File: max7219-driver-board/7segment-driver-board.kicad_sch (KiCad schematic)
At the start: 10 parts, among them IC1 MAX7219CWG, P1 Ext PWR, P2 DataIn, P3 DataOut, P4 Display

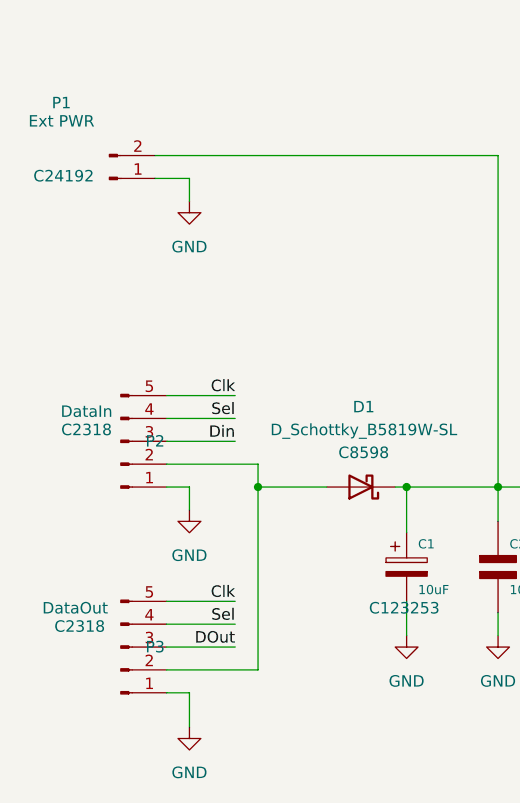
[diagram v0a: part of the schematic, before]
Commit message: changed JST connector to SMD version
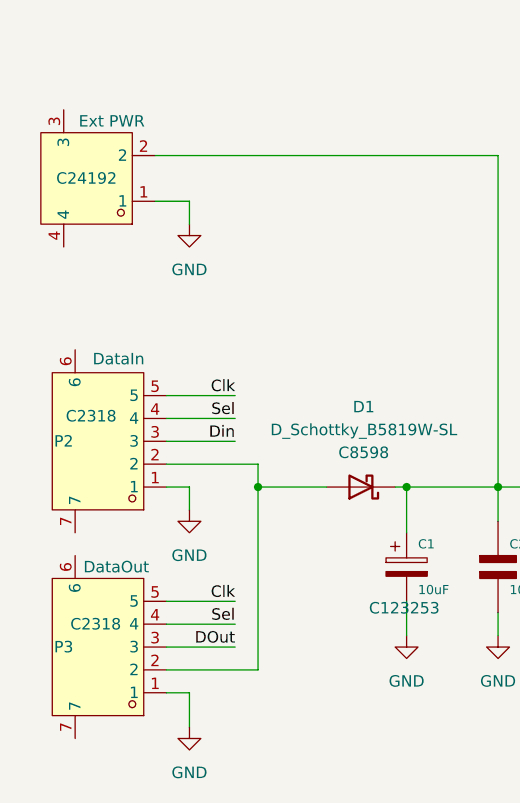
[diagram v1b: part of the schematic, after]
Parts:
- P1: footprint Connector_JST:JST_XH_B2B-XH-A_1x02_P2.50mm_Vertical -> MobiFlight:CONN-SMD_2P-P2.54_XH2.54-2AB; symbol MobiFlight:JST-XH_02_Pin_vertical_red -> MobiFlight:JST-XH2.54-2AB_SMD; LCSC Part (none) -> C146125
- P2, P3: footprint Connector_JST:JST_XH_B5B-XH-A_1x05_P2.50mm_Vertical -> MobiFlight:CONN-SMD_5P-P2.54_XH2.54-5AB; symbol MobiFlight:JST-XH_05_Pin_vertical -> MobiFlight:JST-XH2.54-5AB_SMD; LCSC Part (none) -> C146128
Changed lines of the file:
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@@
 		(title "7 Segment Driver Module")
 		(date "2025-11")
-		(rev "1.0")
+		(rev "1.1")
 	)
 	(junction
@@
 	(wire
 		(pts
-			(xy 55.88 68.58) (xy 59.69 68.58)
+			(xy 55.88 71.12) (xy 59.69 71.12)
 		)
 		(stroke
@@
 	(wire
 		(pts
-			(xy 59.69 68.58) (xy 59.69 71.12)
+			(xy 59.69 71.12) (xy 59.69 73.66)
 		)
 		(stroke
@@
 	)
 	(symbol
-		(lib_id "MobiFlight:JST-XH_05_Pin_vertical")
-		(at 52.07 97.79 0)
-		(mirror x)
+		(lib_id "MobiFlight:JST-XH2.54-5AB_SMD")
+		(at 49.53 97.79 180)
 		(unit 1)
 		(exclude_from_sim no)
@@
 		(dnp no)
 		(property "Reference" "P2"
-			(at 55.88 97.79 0)
+			(at 45.72 97.79 0)
 			(effects
 				(font
@@
 		)
 		(property "Value" "DataIn"
-			(at 48.26 94.488 0)
-			(effects
-				(font
-					(size 1.27 1.27)
-				)
-			)
-		)
-		(property "Footprint" "Connector_JST:JST_XH_B5B-XH-A_1x05_P2.50mm_Vertical"
-			(at 52.07 97.79 0)
-			(effects
-				(font
-					(size 1.27 1.27)
-				)
-				(hide yes)
-			)
-		)
-		(property "Datasheet" "~"
-			(at 52.07 97.79 0)
+			(at 51.816 88.646 0)
+			(effects
+				(font
+					(size 1.27 1.27)
+				)
+			)
+		)
+		(property "Footprint" "MobiFlight:CONN-SMD_5P-P2.54_XH2.54-5AB"
+			(at 49.53 80.01 0)
+			(effects
+				(font
+					(size 1.27 1.27)
+				)
+				(hide yes)
+			)
+		)
+		(property "Datasheet" "https://lcsc.com/product-detail/XH-Connectors_XHsocket-1-5P-2-54mm_C146128.html"
+			(at 49.53 77.47 0)
 			(effects
 				(font
@@
 		)
 		(property "Description" "Generic connector, single row, 01x05, script generated"
-			(at 52.07 97.79 0)
+			(at 49.53 97.79 0)
 			(effects
 				(font
@@
 		)
 		(property "LCSC" "C2318"
-			(at 48.26 96.52 0)
-			(effects
-				(font
-					(size 1.27 1.27)
-				)
+			(at 48.768 94.996 0)
+			(effects
+				(font
+					(size 1.27 1.27)
+				)
+			)
+		)
+		(property "LCSC Part" "C146128"
+			(at 49.53 74.93 0)
+			(effects
+				(font
+					(size 1.27 1.27)
+				)
+				(hide yes)
 			)
 		)
@@
 		)
 		(pin "5"
+		)
+		(pin "7"
+		)
+		(pin "6"
 		)
 		(instances
@@
 	)
 	(symbol
-		(lib_id "MobiFlight:JST-XH_05_Pin_vertical")
-		(at 52.07 120.65 0)
-		(mirror x)
+		(lib_id "MobiFlight:JST-XH2.54-5AB_SMD")
+		(at 49.53 120.65 180)
 		(unit 1)
 		(exclude_from_sim no)
@@
 		(dnp no)
 		(property "Reference" "P3"
-			(at 55.88 120.65 0)
+			(at 45.72 120.65 0)
 			(effects
 				(font
@@
 		)
 		(property "Value" "DataOut"
-			(at 46.99 116.332 0)
-			(effects
-				(font
-					(size 1.27 1.27)
-				)
-			)
-		)
-		(property "Footprint" "Connector_JST:JST_XH_B5B-XH-A_1x05_P2.50mm_Vertical"
-			(at 52.07 120.65 0)
-			(effects
-				(font
-					(size 1.27 1.27)
-				)
-				(hide yes)
-			)
-		)
-		(property "Datasheet" "~"
-			(at 52.07 120.65 0)
+			(at 51.562 111.76 0)
+			(effects
+				(font
+					(size 1.27 1.27)
+				)
+			)
+		)
+		(property "Footprint" "MobiFlight:CONN-SMD_5P-P2.54_XH2.54-5AB"
+			(at 49.53 102.87 0)
+			(effects
+				(font
+					(size 1.27 1.27)
+				)
+				(hide yes)
+			)
+		)
+		(property "Datasheet" "https://lcsc.com/product-detail/XH-Connectors_XHsocket-1-5P-2-54mm_C146128.html"
+			(at 49.53 100.33 0)
 			(effects
 				(font
@@
 		)
 		(property "Description" "Generic connector, single row, 01x05, script generated"
-			(at 52.07 120.65 0)
+			(at 49.53 120.65 0)
 			(effects
 				(font
@@
 		)
 		(property "LCSC" "C2318"
-			(at 47.498 118.364 0)
-			(effects
-				(font
-					(size 1.27 1.27)
-				)
+			(at 49.276 118.11 0)
+			(effects
+				(font
+					(size 1.27 1.27)
+				)
+			)
+		)
+		(property "LCSC Part" "C146128"
+			(at 49.53 97.79 0)
+			(effects
+				(font
+					(size 1.27 1.27)
+				)
+				(hide yes)
 			)
 		)
@@
 		)
 		(pin "5"
+		)
+		(pin "7"
+		)
+		(pin "6"
 		)
 		(instances
@@
 	)
 	(symbol
-		(lib_id "MobiFlight:JST-XH_02_Pin_vertical_red")
-		(at 50.8 68.58 0)
-		(mirror x)
+		(lib_id "MobiFlight:JST-XH2.54-2AB_SMD")
+		(at 48.26 68.58 180)
 		(unit 1)
 		(exclude_from_sim no)
@@
 		(dnp no)
 		(property "Reference" "P1"
-			(at 45.466 60.198 0)
-			(effects
-				(font
-					(size 1.27 1.27)
-				)
+			(at 49.53 60.452 0)
+			(effects
+				(font
+					(size 1.27 1.27)
+				)
+				(hide yes)
 			)
 		)
 		(property "Value" "Ext PWR"
-			(at 45.466 62.23 0)
-			(effects
-				(font
-					(size 1.27 1.27)
-				)
-			)
-		)
-		(property "Footprint" "Connector_JST:JST_XH_B2B-XH-A_1x02_P2.50mm_Vertical"
-			(at 50.8 68.58 0)
-			(effects
-				(font
-					(size 1.27 1.27)
-				)
-				(hide yes)
-			)
-		)
-		(property "Datasheet" "~"
-			(at 50.8 68.58 0)
+			(at 51.054 62.23 0)
+			(effects
+				(font
+					(size 1.27 1.27)
+				)
+			)
+		)
+		(property "Footprint" "MobiFlight:CONN-SMD_2P-P2.54_XH2.54-2AB"
+			(at 48.26 53.34 0)
+			(effects
+				(font
+					(size 1.27 1.27)
+				)
+				(hide yes)
+			)
+		)
+		(property "Datasheet" "https://lcsc.com/product-detail/XH-Connectors_XHsocket-1-2P-2-54mm_C146125.html"
+			(at 48.26 50.8 0)
 			(effects
 				(font
@@
 		)
 		(property "Description" "Generic connector, single row, 01x02, script generated"
-			(at 50.8 68.58 0)
+			(at 48.26 68.58 0)
 			(effects
 				(font
@@
 		)
 		(property "LCSC" "C24192"
-			(at 45.72 68.326 0)
-			(effects
-				(font
-					(size 1.27 1.27)
-				)
+			(at 48.26 68.58 0)
+			(effects
+				(font
+					(size 1.27 1.27)
+				)
+			)
+		)
+		(property "LCSC Part" "C146125"
+			(at 48.26 48.26 0)
+			(effects
+				(font
+					(size 1.27 1.27)
+				)
+				(hide yes)
 			)
 		)
@@
 		)
 		(pin "2"
+		)
+		(pin "4"
+		)
+		(pin "3"
 		)
 		(instances
@@
 	(symbol
 		(lib_id "power:GND")
-		(at 59.69 71.12 0)
+		(at 59.69 73.66 0)
 		(unit 1)
 		(exclude_from_sim no)
@@
 		(fields_autoplaced yes)
 		(property "Reference" "#PWR02"
-			(at 59.69 77.47 0)
+			(at 59.69 80.01 0)
 			(effects
 				(font
@@
 		)
 		(property "Value" "GND"
-			(at 59.69 76.2 0)
+			(at 59.69 78.74 0)
 			(effects
 				(font
@@
 		)
 		(property "Footprint" ""
-			(at 59.69 71.12 0)
+			(at 59.69 73.66 0)
 			(effects
 				(font
@@
 		)
 		(property "Datasheet" ""
-			(at 59.69 71.12 0)
+			(at 59.69 73.66 0)
 			(effects
 				(font
@@
 		)
 		(property "Description" "Power symbol creates a global label with name \"GND\" , ground"
-			(at 59.69 71.12 0)
-			(effects
-				(font
+			(at 59.69 73.66 0)
+			(effects
+				(font
